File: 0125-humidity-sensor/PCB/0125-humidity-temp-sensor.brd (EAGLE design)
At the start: 6 x 6 mm, 8 parts

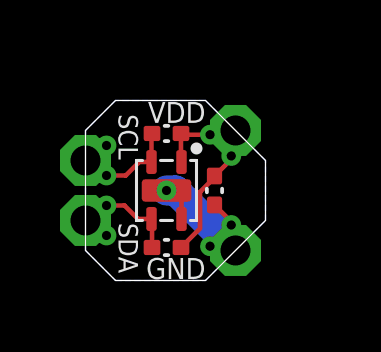
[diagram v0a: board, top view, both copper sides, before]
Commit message: Big batch of new PCBs sent to FAB.
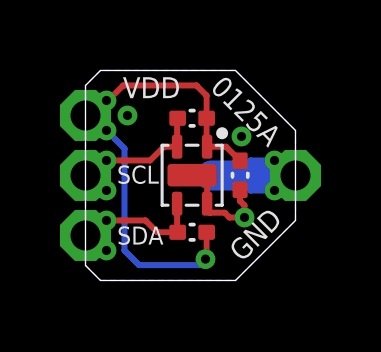
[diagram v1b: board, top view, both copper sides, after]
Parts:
- R1, R2: value 4.7K -> XXX
- moved VDD 5.02 mm to (0.00, 5.50), turned to 180 degrees
- moved GND 3.20 mm to (7.00, 3.50), turned to 0 degrees
- moved C1 0.99 mm to (5.15, 3.51)
- moved R1 0.99 mm to (3.55, 5.41)
- moved R2 0.99 mm to (3.55, 1.61)
- moved TH1 0.99 mm to (3.55, 3.51)
- moved SCL 0.50 mm to (0.00, 3.50)
- moved SDA 0.50 mm to (0.00, 1.50)
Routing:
- net VDD: track 7.30 -> 18.5 mm, vias 0 -> 1
- net GND: track 7.31 -> 13.3 mm, vias 1 -> 3
- net SCL: track 4.46 -> 5.32 mm
- net SDA: track 4.46 -> 5.31 mm
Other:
- board size 6 x 6 mm -> 7 x 7 mm
